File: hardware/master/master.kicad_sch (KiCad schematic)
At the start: 0 parts

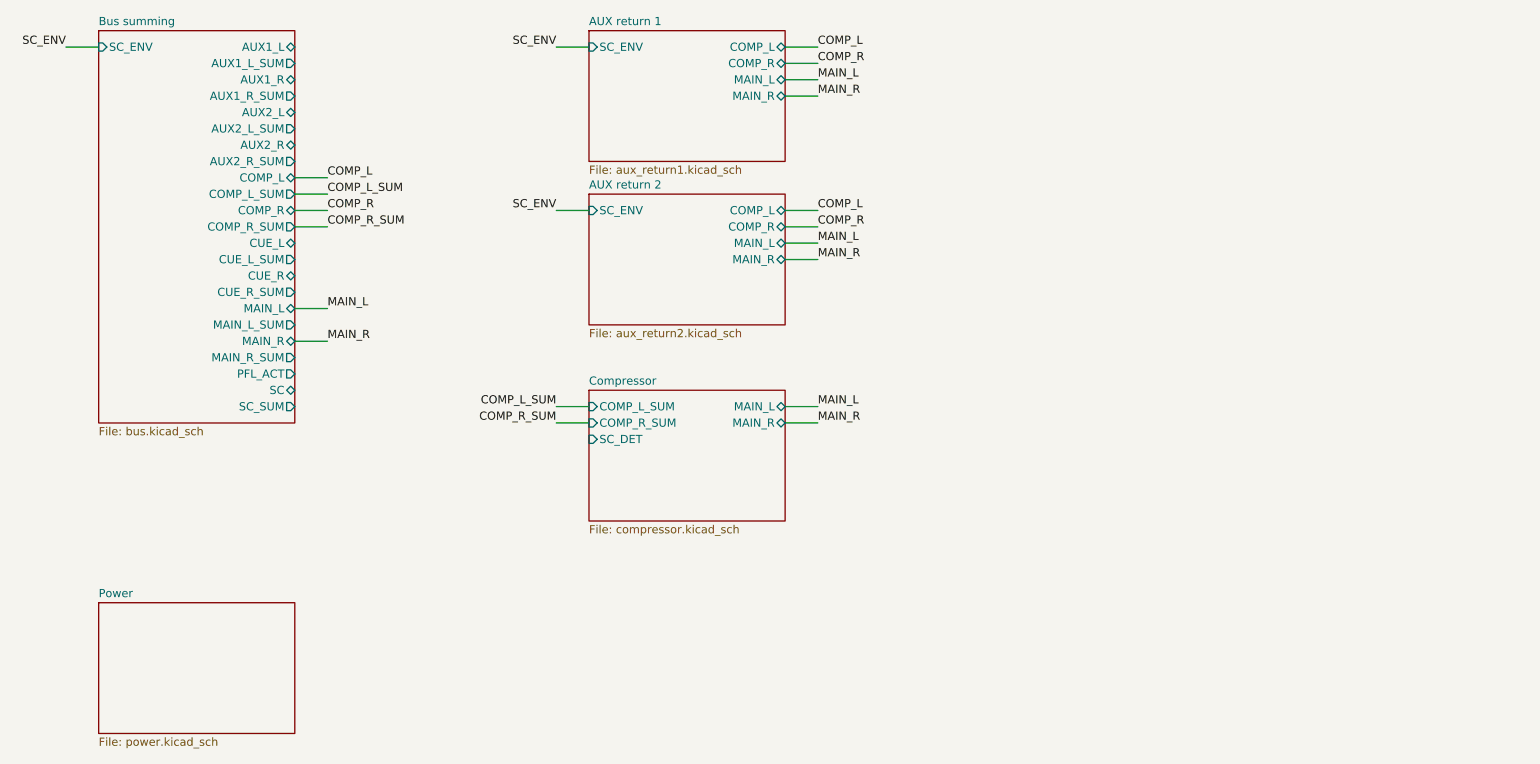
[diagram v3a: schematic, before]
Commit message: Add master card sidechain and ducking sheet
Source selection by an SC BUS button with EXT plug override, Sallen-Key
sidechain LPF (46-510 Hz) with bypass, SC listen to the cue buses with
the PFL_ACT driver, and a trigger-style ducker driving SC_ENV
(decision 90). Filter and ducker simulated in ngspice
(simulation/sidechain).

Co-Authored-By: Claude Opus 5.5 <noreply@anthropic.com>
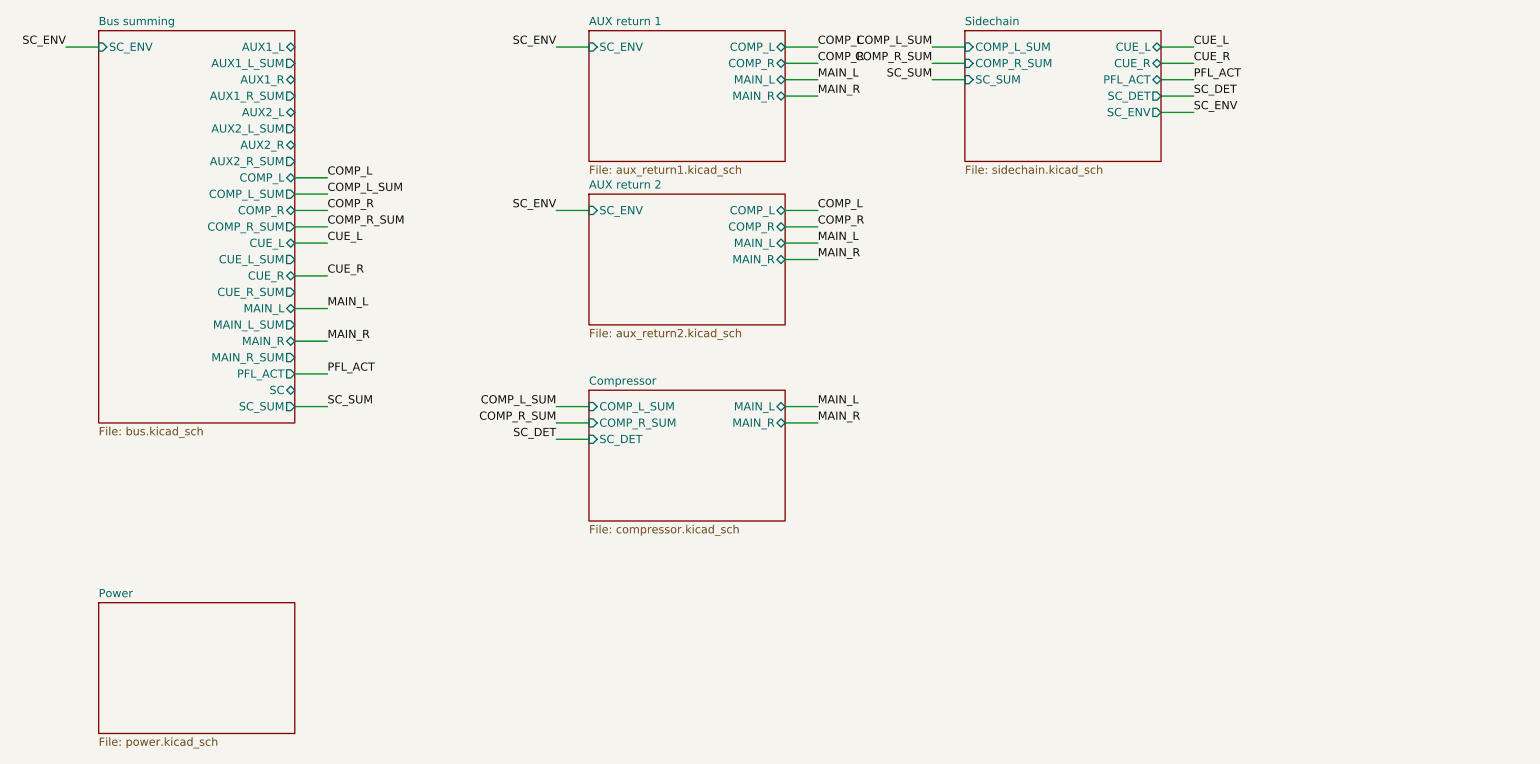
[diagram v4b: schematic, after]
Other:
- added sheet Sidechain (sidechain.kicad_sch)
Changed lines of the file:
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@@
 		)
 		(pin "MAIN_L" bidirectional
-			(at 132.08 96.52 0)
+			(at 132.08 96.52 0.0000)
 			(effects
 				(font
@@
 		)
 		(pin "MAIN_R" bidirectional
-			(at 132.08 99.06 0)
+			(at 132.08 99.06 0.0000)
 			(effects
 				(font
@@
 				(path "/e58f7b8d-79d3-4449-9042-9214947ce872"
 					(page "6")
+				)
+			)
+		)
+	)
+	(sheet
+		(at 160.02 38.1)
+		(size 30.48 20.32)
+		(exclude_from_sim no)
+		(in_bom yes)
+		(on_board yes)
+		(dnp no)
+		(fields_autoplaced yes)
+		(stroke
+			(width 0.1524)
+			(type solid)
+		)
+		(fill
+			(color 0 0 0 0.0000)
+		)
+		(property "Sheetname" "Sidechain"
+			(at 160.02 37.3884 0)
+			(effects
+				(font
+					(size 1.27 1.27)
+				)
+				(justify left bottom)
+			)
+		)
+		(property "Sheetfile" "sidechain.kicad_sch"
+			(at 160.02 59.0046 0)
+			(effects
+				(font
+					(size 1.27 1.27)
+				)
+				(justify left top)
+			)
+		)
+		(pin "COMP_L_SUM" input
+			(at 160.02 40.64 180)
+			(effects
+				(font
+					(size 1.27 1.27)
+				)
+				(justify left)
+			)
+		)
+		(pin "COMP_R_SUM" input
+			(at 160.02 43.18 180)
+			(effects
+				(font
+					(size 1.27 1.27)
+				)
+				(justify left)
+			)
+		)
+		(pin "SC_SUM" input
+			(at 160.02 45.72 180)
+			(effects
+				(font
+					(size 1.27 1.27)
+				)
+				(justify left)
+			)
+		)
+		(pin "CUE_L" bidirectional
+			(at 190.5 40.64 0)
+			(effects
+				(font
+					(size 1.27 1.27)
+				)
+				(justify right)
+			)
+		)
+		(pin "CUE_R" bidirectional
+			(at 190.5 43.18 0)
+			(effects
+				(font
+					(size 1.27 1.27)
+				)
+				(justify right)
+			)
+		)
+		(pin "PFL_ACT" bidirectional
+			(at 190.5 45.72 0)
+			(effects
+				(font
+					(size 1.27 1.27)
+				)
+				(justify right)
+			)
+		)
+		(pin "SC_DET" output
+			(at 190.5 48.26 0)
+			(effects
+				(font
+					(size 1.27 1.27)
+				)
+				(justify right)
+			)
+		)
+		(pin "SC_ENV" output
+			(at 190.5 50.8 0)
+			(effects
+				(font
+					(size 1.27 1.27)
+				)
+				(justify right)
+			)
+		)
+		(instances
+			(project "master"
+				(path "/e58f7b8d-79d3-4449-9042-9214947ce872"
+					(page "7")
 				)
 			)
@@
 	(wire (pts (xy 55.88 68.58) (xy 60.96 68.58)) (stroke (width 0) (type default)))
 	(label "COMP_R_SUM" (at 60.96 68.58 0) (fields_autoplaced yes) (effects (font (size 1.27 1.27)) (justify left bottom)))
+	(wire (pts (xy 55.88 71.12) (xy 60.96 71.12)) (stroke (width 0) (type default)))
+	(label "CUE_L" (at 60.96 71.12 0) (fields_autoplaced yes) (effects (font (size 1.27 1.27)) (justify left bottom)))
+	(wire (pts (xy 55.88 76.2) (xy 60.96 76.2)) (stroke (width 0) (type default)))
+	(label "CUE_R" (at 60.96 76.2 0) (fields_autoplaced yes) (effects (font (size 1.27 1.27)) (justify left bottom)))
 	(wire (pts (xy 55.88 81.28) (xy 60.96 81.28)) (stroke (width 0) (type default)))
 	(label "MAIN_L" (at 60.96 81.28 0) (fields_autoplaced yes) (effects (font (size 1.27 1.27)) (justify left bottom)))
 	(wire (pts (xy 55.88 86.36) (xy 60.96 86.36)) (stroke (width 0) (type default)))
 	(label "MAIN_R" (at 60.96 86.36 0) (fields_autoplaced yes) (effects (font (size 1.27 1.27)) (justify left bottom)))
+	(wire (pts (xy 55.88 91.44) (xy 60.96 91.44)) (stroke (width 0) (type default)))
+	(label "PFL_ACT" (at 60.96 91.44 0) (fields_autoplaced yes) (effects (font (size 1.27 1.27)) (justify left bottom)))
+	(wire (pts (xy 55.88 96.52) (xy 60.96 96.52)) (stroke (width 0) (type default)))
+	(label "SC_SUM" (at 60.96 96.52 0) (fields_autoplaced yes) (effects (font (size 1.27 1.27)) (justify left bottom)))
 	(wire (pts (xy 101.6 40.64) (xy 96.52 40.64)) (stroke (width 0) (type default)))
 	(label "SC_ENV" (at 96.52 40.64 180) (fields_autoplaced yes) (effects (font (size 1.27 1.27)) (justify right bottom)))
@@
 	(wire (pts (xy 101.6 99.06) (xy 96.52 99.06)) (stroke (width 0) (type default)))
 	(label "COMP_R_SUM" (at 96.52 99.06 180) (fields_autoplaced yes) (effects (font (size 1.27 1.27)) (justify right bottom)))
+	(wire (pts (xy 101.6 101.6) (xy 96.52 101.6)) (stroke (width 0) (type default)))
+	(label "SC_DET" (at 96.52 101.6 180) (fields_autoplaced yes) (effects (font (size 1.27 1.27)) (justify right bottom)))
 	(wire (pts (xy 132.08 96.52) (xy 137.16 96.52)) (stroke (width 0) (type default)))
 	(label "MAIN_L" (at 137.16 96.52 0) (fields_autoplaced yes) (effects (font (size 1.27 1.27)) (justify left bottom)))
 	(wire (pts (xy 132.08 99.06) (xy 137.16 99.06)) (stroke (width 0) (type default)))
 	(label "MAIN_R" (at 137.16 99.06 0) (fields_autoplaced yes) (effects (font (size 1.27 1.27)) (justify left bottom)))
+	(wire (pts (xy 160.02 40.64) (xy 154.94 40.64)) (stroke (width 0) (type default)))
+	(label "COMP_L_SUM" (at 154.94 40.64 180) (fields_autoplaced yes) (effects (font (size 1.27 1.27)) (justify right bottom)))
+	(wire (pts (xy 160.02 43.18) (xy 154.94 43.18)) (stroke (width 0) (type default)))
+	(label "COMP_R_SUM" (at 154.94 43.18 180) (fields_autoplaced yes) (effects (font (size 1.27 1.27)) (justify right bottom)))
+	(wire (pts (xy 160.02 45.72) (xy 154.94 45.72)) (stroke (width 0) (type default)))
+	(label "SC_SUM" (at 154.94 45.72 180) (fields_autoplaced yes) (effects (font (size 1.27 1.27)) (justify right bottom)))
+	(wire (pts (xy 190.5 40.64) (xy 195.58 40.64)) (stroke (width 0) (type default)))
+	(label "CUE_L" (at 195.58 40.64 0) (fields_autoplaced yes) (effects (font (size 1.27 1.27)) (justify left bottom)))
+	(wire (pts (xy 190.5 43.18) (xy 195.58 43.18)) (stroke (width 0) (type default)))
+	(label "CUE_R" (at 195.58 43.18 0) (fields_autoplaced yes) (effects (font (size 1.27 1.27)) (justify left bottom)))
+	(wire (pts (xy 190.5 45.72) (xy 195.58 45.72)) (stroke (width 0) (type default)))
+	(label "PFL_ACT" (at 195.58 45.72 0) (fields_autoplaced yes) (effects (font (size 1.27 1.27)) (justify left bottom)))
+	(wire (pts (xy 190.5 48.26) (xy 195.58 48.26)) (stroke (width 0) (type default)))
+	(label "SC_DET" (at 195.58 48.26 0) (fields_autoplaced yes) (effects (font (size 1.27 1.27)) (justify left bottom)))
+	(wire (pts (xy 190.5 50.8) (xy 195.58 50.8)) (stroke (width 0) (type default)))
+	(label "SC_ENV" (at 195.58 50.8 0) (fields_autoplaced yes) (effects (font (size 1.27 1.27)) (justify left bottom)))
 	(sheet_instances
 		(path "/"

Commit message: Add master card AUX sends sheet
Dual-gang send masters with polarity-restoring 47k inverters,
impedance-balanced TRS outputs and L/MONO summing switched by a DG411
from the R jack's plug detection (decision 91).

Co-Authored-By: Claude Opus 5.5 <noreply@anthropic.com>
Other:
- added sheet AUX sends (aux_sends.kicad_sch)
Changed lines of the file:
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@@
 		)
 		(pin "CUE_L" bidirectional
-			(at 190.5 40.64 0)
+			(at 190.5 40.64 0.0000)
 			(effects
 				(font
@@
 		)
 		(pin "CUE_R" bidirectional
-			(at 190.5 43.18 0)
+			(at 190.5 43.18 0.0000)
 			(effects
 				(font
@@
 		)
 		(pin "PFL_ACT" bidirectional
-			(at 190.5 45.72 0)
+			(at 190.5 45.72 0.0000)
 			(effects
 				(font
@@
 		)
 		(pin "SC_DET" output
-			(at 190.5 48.26 0)
+			(at 190.5 48.26 0.0000)
 			(effects
 				(font
@@
 		)
 		(pin "SC_ENV" output
-			(at 190.5 50.8 0)
+			(at 190.5 50.8 0.0000)
 			(effects
 				(font
@@
 		)
 	)
+	(sheet
+		(at 160.02 63.5)
+		(size 30.48 20.32)
+		(exclude_from_sim no)
+		(in_bom yes)
+		(on_board yes)
+		(dnp no)
+		(fields_autoplaced yes)
+		(stroke
+			(width 0.1524)
+			(type solid)
+		)
+		(fill
+			(color 0 0 0 0.0000)
+		)
+		(property "Sheetname" "AUX sends"
+			(at 160.02 62.7884 0)
+			(effects
+				(font
+					(size 1.27 1.27)
+				)
+				(justify left bottom)
+			)
+		)
+		(property "Sheetfile" "aux_sends.kicad_sch"
+			(at 160.02 84.4046 0)
+			(effects
+				(font
+					(size 1.27 1.27)
+				)
+				(justify left top)
+			)
+		)
+		(pin "AUX1_L_SUM" input
+			(at 160.02 66.04 180)
+			(effects
+				(font
+					(size 1.27 1.27)
+				)
+				(justify left)
+			)
+		)
+		(pin "AUX1_R_SUM" input
+			(at 160.02 68.58 180)
+			(effects
+				(font
+					(size 1.27 1.27)
+				)
+				(justify left)
+			)
+		)
+		(pin "AUX2_L_SUM" input
+			(at 160.02 71.12 180)
+			(effects
+				(font
+					(size 1.27 1.27)
+				)
+				(justify left)
+			)
+		)
+		(pin "AUX2_R_SUM" input
+			(at 160.02 73.66 180)
+			(effects
+				(font
+					(size 1.27 1.27)
+				)
+				(justify left)
+			)
+		)
+		(instances
+			(project "master"
+				(path "/e58f7b8d-79d3-4449-9042-9214947ce872"
+					(page "8")
+				)
+			)
+		)
+	)
 	(wire (pts (xy 25.4 40.64) (xy 20.32 40.64)) (stroke (width 0) (type default)))
 	(label "SC_ENV" (at 20.32 40.64 180) (fields_autoplaced yes) (effects (font (size 1.27 1.27)) (justify right bottom)))
+	(wire (pts (xy 55.88 43.18) (xy 60.96 43.18)) (stroke (width 0) (type default)))
+	(label "AUX1_L_SUM" (at 60.96 43.18 0) (fields_autoplaced yes) (effects (font (size 1.27 1.27)) (justify left bottom)))
+	(wire (pts (xy 55.88 48.26) (xy 60.96 48.26)) (stroke (width 0) (type default)))
+	(label "AUX1_R_SUM" (at 60.96 48.26 0) (fields_autoplaced yes) (effects (font (size 1.27 1.27)) (justify left bottom)))
+	(wire (pts (xy 55.88 53.34) (xy 60.96 53.34)) (stroke (width 0) (type default)))
+	(label "AUX2_L_SUM" (at 60.96 53.34 0) (fields_autoplaced yes) (effects (font (size 1.27 1.27)) (justify left bottom)))
+	(wire (pts (xy 55.88 58.42) (xy 60.96 58.42)) (stroke (width 0) (type default)))
+	(label "AUX2_R_SUM" (at 60.96 58.42 0) (fields_autoplaced yes) (effects (font (size 1.27 1.27)) (justify left bottom)))
 	(wire (pts (xy 55.88 60.96) (xy 60.96 60.96)) (stroke (width 0) (type default)))
 	(label "COMP_L" (at 60.96 60.96 0) (fields_autoplaced yes) (effects (font (size 1.27 1.27)) (justify left bottom)))
@@
 	(wire (pts (xy 190.5 50.8) (xy 195.58 50.8)) (stroke (width 0) (type default)))
 	(label "SC_ENV" (at 195.58 50.8 0) (fields_autoplaced yes) (effects (font (size 1.27 1.27)) (justify left bottom)))
+	(wire (pts (xy 160.02 66.04) (xy 154.94 66.04)) (stroke (width 0) (type default)))
+	(label "AUX1_L_SUM" (at 154.94 66.04 180) (fields_autoplaced yes) (effects (font (size 1.27 1.27)) (justify right bottom)))
+	(wire (pts (xy 160.02 68.58) (xy 154.94 68.58)) (stroke (width 0) (type default)))
+	(label "AUX1_R_SUM" (at 154.94 68.58 180) (fields_autoplaced yes) (effects (font (size 1.27 1.27)) (justify right bottom)))
+	(wire (pts (xy 160.02 71.12) (xy 154.94 71.12)) (stroke (width 0) (type default)))
+	(label "AUX2_L_SUM" (at 154.94 71.12 180) (fields_autoplaced yes) (effects (font (size 1.27 1.27)) (justify right bottom)))
+	(wire (pts (xy 160.02 73.66) (xy 154.94 73.66)) (stroke (width 0) (type default)))
+	(label "AUX2_R_SUM" (at 154.94 73.66 180) (fields_autoplaced yes) (effects (font (size 1.27 1.27)) (justify right bottom)))
 	(sheet_instances
 		(path "/"

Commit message: Add master card master out sheet
SSI2162 master VCA with the channel fader law, soft clip in the I-V
stages, THAT1646 balanced drivers with offset caps and phantom clamps,
G6K output protection relays with 2 s power-up delay and raw-rail
drop-out (decision 92). Adds the THAT1646 symbol and exports
+20V_RAW from the power sheet.

Co-Authored-By: Claude Opus 5.5 <noreply@anthropic.com>
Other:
- added sheet Master out (master_out.kicad_sch)
- sheet Power ports: added +20V_RAW; removed none
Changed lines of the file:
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@@
+			)
+		)
+		(pin "+20V_RAW" output
+			(at 55.88 129.54 0.0000)
+			(effects
+				(font
+					(size 1.27 1.27)
+				)
+				(justify right)
 			)
 		)
@@
 				(path "/e58f7b8d-79d3-4449-9042-9214947ce872"
 					(page "8")
+				)
+			)
+		)
+	)
+	(sheet
+		(at 160.02 93.98)
+		(size 30.48 20.32)
+		(exclude_from_sim no)
+		(in_bom yes)
+		(on_board yes)
+		(dnp no)
+		(fields_autoplaced yes)
+		(stroke
+			(width 0.1524)
+			(type solid)
+		)
+		(fill
+			(color 0 0 0 0.0000)
+		)
+		(property "Sheetname" "Master out"
+			(at 160.02 93.2684 0)
+			(effects
+				(font
+					(size 1.27 1.27)
+				)
+				(justify left bottom)
+			)
+		)
+		(property "Sheetfile" "master_out.kicad_sch"
+			(at 160.02 114.8846 0)
+			(effects
+				(font
+					(size 1.27 1.27)
+				)
+				(justify left top)
+			)
+		)
+		(pin "+20V_RAW" input
+			(at 160.02 96.52 180)
+			(effects
+				(font
+					(size 1.27 1.27)
+				)
+				(justify left)
+			)
+		)
+		(pin "MAIN_L_SUM" input
+			(at 160.02 99.06 180)
+			(effects
+				(font
+					(size 1.27 1.27)
+				)
+				(justify left)
+			)
+		)
+		(pin "MAIN_R_SUM" input
+			(at 160.02 101.6 180)
+			(effects
+				(font
+					(size 1.27 1.27)
+				)
+				(justify left)
+			)
+		)
+		(pin "MAIN_L_OUT" output
+			(at 190.5 96.52 0)
+			(effects
+				(font
+					(size 1.27 1.27)
+				)
+				(justify right)
+			)
+		)
+		(pin "MAIN_R_OUT" output
+			(at 190.5 99.06 0)
+			(effects
+				(font
+					(size 1.27 1.27)
+				)
+				(justify right)
+			)
+		)
+		(pin "RLY_N" output
+			(at 190.5 101.6 0)
+			(effects
+				(font
+					(size 1.27 1.27)
+				)
+				(justify right)
+			)
+		)
+		(instances
+			(project "master"
+				(path "/e58f7b8d-79d3-4449-9042-9214947ce872"
+					(page "9")
 				)
 			)
@@
 	(wire (pts (xy 55.88 81.28) (xy 60.96 81.28)) (stroke (width 0) (type default)))
 	(label "MAIN_L" (at 60.96 81.28 0) (fields_autoplaced yes) (effects (font (size 1.27 1.27)) (justify left bottom)))
+	(wire (pts (xy 55.88 83.82) (xy 60.96 83.82)) (stroke (width 0) (type default)))
+	(label "MAIN_L_SUM" (at 60.96 83.82 0) (fields_autoplaced yes) (effects (font (size 1.27 1.27)) (justify left bottom)))
 	(wire (pts (xy 55.88 86.36) (xy 60.96 86.36)) (stroke (width 0) (type default)))
 	(label "MAIN_R" (at 60.96 86.36 0) (fields_autoplaced yes) (effects (font (size 1.27 1.27)) (justify left bottom)))
+	(wire (pts (xy 55.88 88.9) (xy 60.96 88.9)) (stroke (width 0) (type default)))
+	(label "MAIN_R_SUM" (at 60.96 88.9 0) (fields_autoplaced yes) (effects (font (size 1.27 1.27)) (justify left bottom)))
 	(wire (pts (xy 55.88 91.44) (xy 60.96 91.44)) (stroke (width 0) (type default)))
 	(label "PFL_ACT" (at 60.96 91.44 0) (fields_autoplaced yes) (effects (font (size 1.27 1.27)) (justify left bottom)))
 	(wire (pts (xy 55.88 96.52) (xy 60.96 96.52)) (stroke (width 0) (type default)))
 	(label "SC_SUM" (at 60.96 96.52 0) (fields_autoplaced yes) (effects (font (size 1.27 1.27)) (justify left bottom)))
+	(wire (pts (xy 55.88 129.54) (xy 60.96 129.54)) (stroke (width 0) (type default)))
+	(label "+20V_RAW" (at 60.96 129.54 0) (fields_autoplaced yes) (effects (font (size 1.27 1.27)) (justify left bottom)))
 	(wire (pts (xy 101.6 40.64) (xy 96.52 40.64)) (stroke (width 0) (type default)))
 	(label "SC_ENV" (at 96.52 40.64 180) (fields_autoplaced yes) (effects (font (size 1.27 1.27)) (justify right bottom)))
@@
 	(wire (pts (xy 160.02 73.66) (xy 154.94 73.66)) (stroke (width 0) (type default)))
 	(label "AUX2_R_SUM" (at 154.94 73.66 180) (fields_autoplaced yes) (effects (font (size 1.27 1.27)) (justify right bottom)))
+	(wire (pts (xy 160.02 96.52) (xy 154.94 96.52)) (stroke (width 0) (type default)))
+	(label "+20V_RAW" (at 154.94 96.52 180) (fields_autoplaced yes) (effects (font (size 1.27 1.27)) (justify right bottom)))
+	(wire (pts (xy 160.02 99.06) (xy 154.94 99.06)) (stroke (width 0) (type default)))
+	(label "MAIN_L_SUM" (at 154.94 99.06 180) (fields_autoplaced yes) (effects (font (size 1.27 1.27)) (justify right bottom)))
+	(wire (pts (xy 160.02 101.6) (xy 154.94 101.6)) (stroke (width 0) (type default)))
+	(label "MAIN_R_SUM" (at 154.94 101.6 180) (fields_autoplaced yes) (effects (font (size 1.27 1.27)) (justify right bottom)))
 	(sheet_instances
 		(path "/"
